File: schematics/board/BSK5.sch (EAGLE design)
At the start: 18 parts

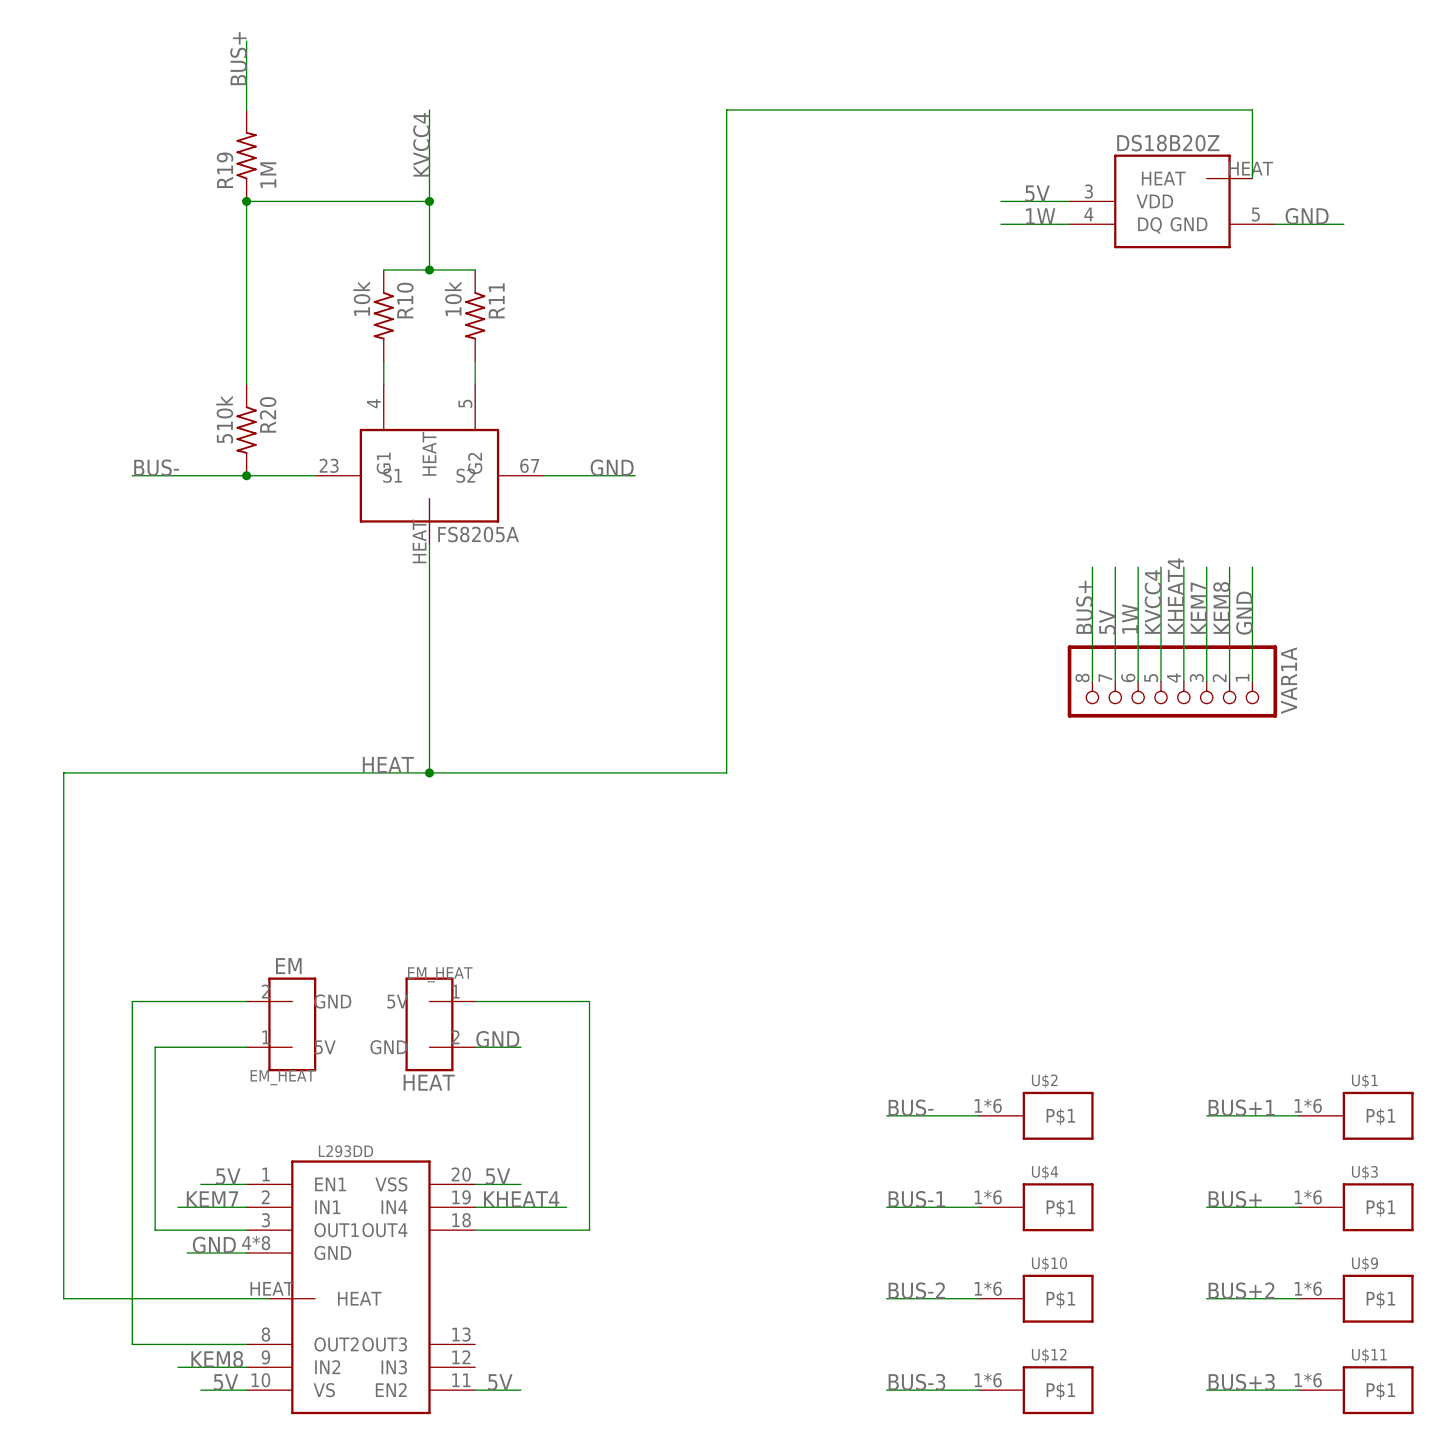
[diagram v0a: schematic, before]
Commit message: Добавлены светодиоды на платы БСК
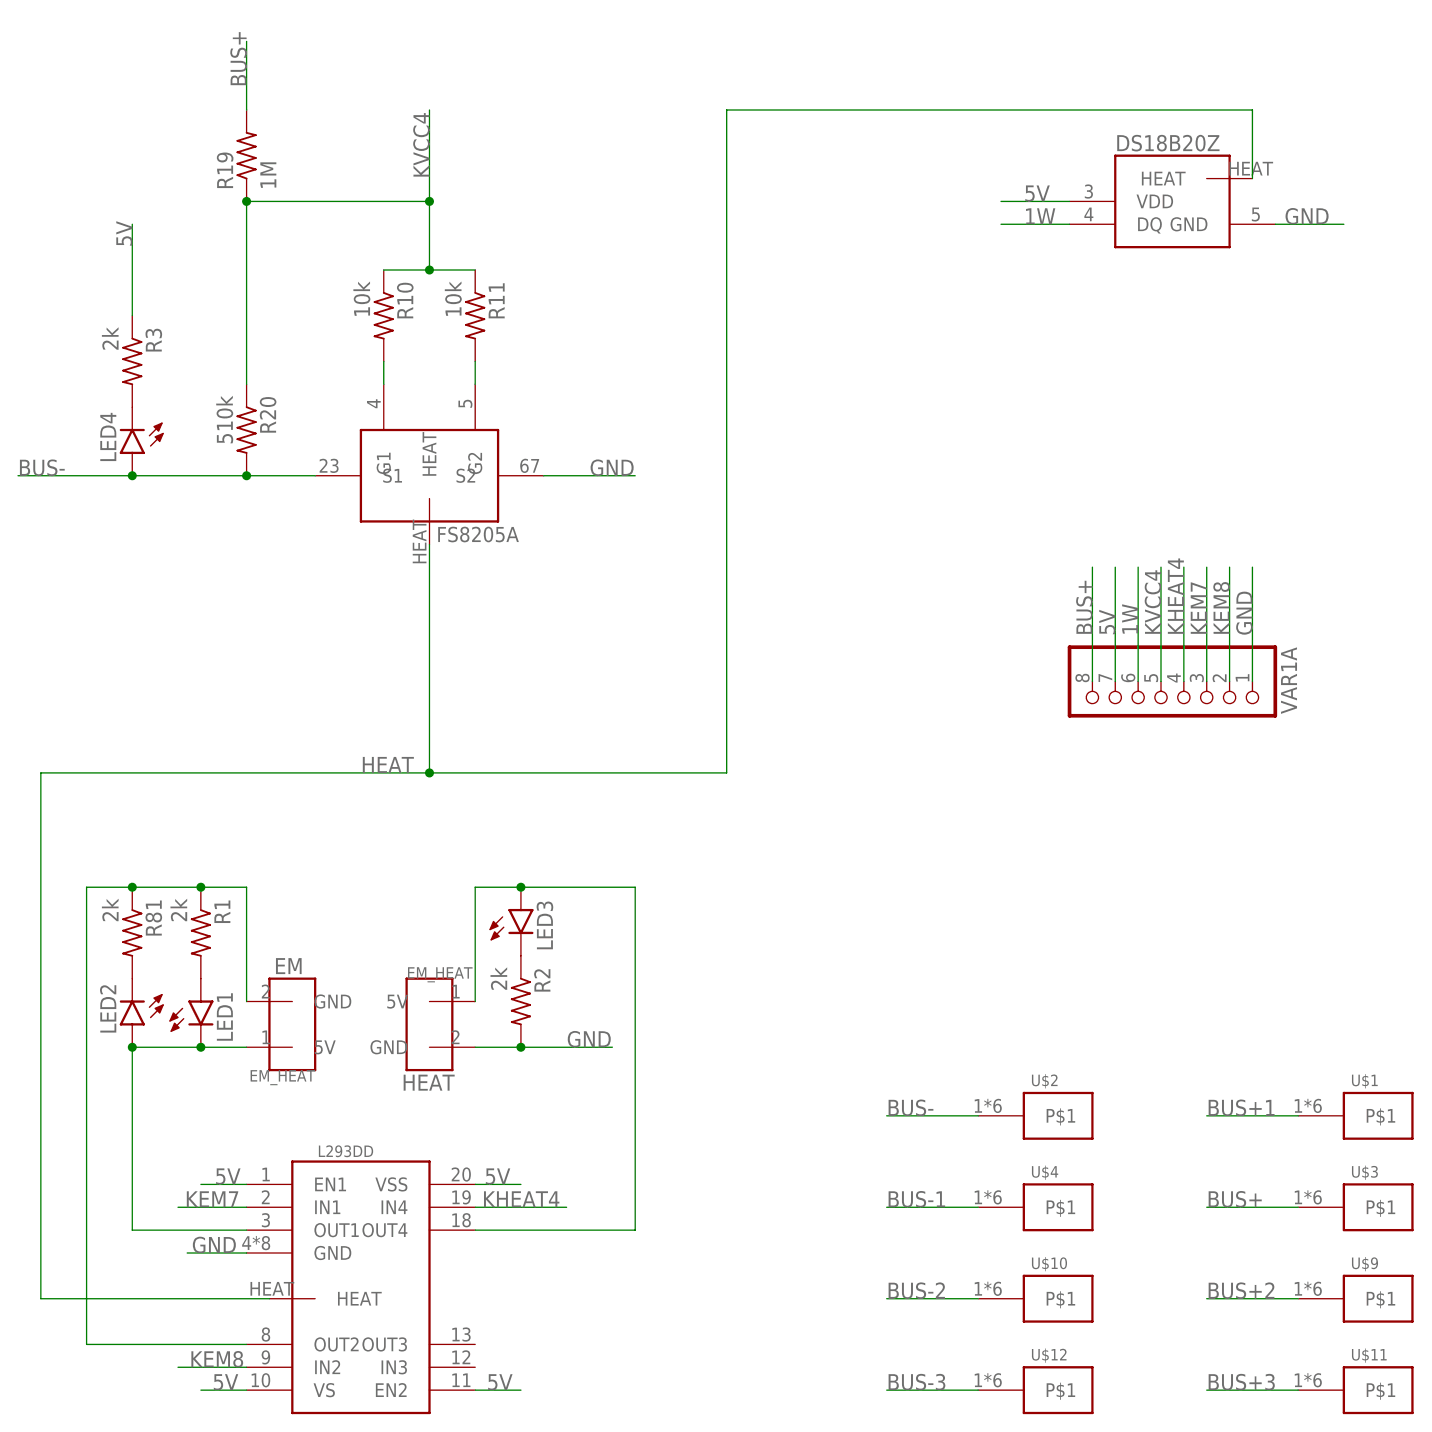
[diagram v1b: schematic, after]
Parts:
- added LED1, LED2, LED3, LED4: (no value), led:LEDCHIPLED_0603
- added R1, R2, R3, R81: 2k, resistor:R-US_R0603
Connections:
- new net N$26: LED2.C, R81.2
- new net N$27: LED1.A, R1.2
- new net N$28: LED3.C, R2.1
- new net N$29: LED4.C, R3.2
- net 5V: now also R3.1
- net BUS-: now also LED4.A
- net GND: now also R2.2
- net N$1: now also LED1.C, LED2.A
- net N$2: now also R1.1, R81.1
- net N$3: now also LED3.A
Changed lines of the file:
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@@
 <part name="U$12" library="CanCubeSat" deviceset="KCONNECT" device=""/>
 <part name="VAR1A" library="pinheadCS" deviceset="PINHD-1X8" device=""/>
+<part name="LED2" library="led" library_urn="urn:adsk.eagle:library:259" deviceset="LED" device="CHIPLED_0603" package3d_urn="urn:adsk.eagle:package:15822/2"/>
+<part name="R81" library="resistor" library_urn="urn:adsk.eagle:library:348" deviceset="R-US_" device="R0603" package3d_urn="urn:adsk.eagle:package:23555/3" value="2k"/>
+<part name="R1" library="resistor" library_urn="urn:adsk.eagle:library:348" deviceset="R-US_" device="R0603" package3d_urn="urn:adsk.eagle:package:23555/3" value="2k"/>
+<part name="LED1" library="led" library_urn="urn:adsk.eagle:library:259" deviceset="LED" device="CHIPLED_0603" package3d_urn="urn:adsk.eagle:package:15822/2"/>
+<part name="R2" library="resistor" library_urn="urn:adsk.eagle:library:348" deviceset="R-US_" device="R0603" package3d_urn="urn:adsk.eagle:package:23555/3" value="2k"/>
+<part name="LED3" library="led" library_urn="urn:adsk.eagle:library:259" deviceset="LED" device="CHIPLED_0603" package3d_urn="urn:adsk.eagle:package:15822/2"/>
+<part name="LED4" library="led" library_urn="urn:adsk.eagle:library:259" deviceset="LED" device="CHIPLED_0603" package3d_urn="urn:adsk.eagle:package:15822/2"/>
+<part name="R3" library="resistor" library_urn="urn:adsk.eagle:library:348" deviceset="R-US_" device="R0603" package3d_urn="urn:adsk.eagle:package:23555/3" value="2k"/>
 </parts>
 <sheets>
@@
 <attribute name="VALUE" x="142.24" y="181.61" size="1.778" layer="96" rot="R270"/>
 </instance>
+<instance part="LED2" gate="G$1" x="40.64" y="139.7" smashed="yes" rot="R180">
+<attribute name="NAME" x="37.084" y="144.272" size="1.778" layer="95" rot="R270"/>
+<attribute name="VALUE" x="34.925" y="144.272" size="1.778" layer="96" rot="R270"/>
+</instance>
+<instance part="R81" gate="G$1" x="40.64" y="149.86" smashed="yes" rot="R270">
+<attribute name="NAME" x="42.1386" y="153.67" size="1.778" layer="95" rot="R270"/>
+<attribute name="VALUE" x="37.338" y="153.67" size="1.778" layer="96" rot="R270"/>
+</instance>
+<instance part="R1" gate="G$1" x="48.26" y="149.86" smashed="yes" rot="R270">
+<attribute name="NAME" x="49.7586" y="153.67" size="1.778" layer="95" rot="R270"/>
+<attribute name="VALUE" x="44.958" y="153.67" size="1.778" layer="96" rot="R270"/>
+</instance>
+<instance part="LED1" gate="G$1" x="48.26" y="142.24" smashed="yes">
+<attribute name="NAME" x="51.816" y="137.668" size="1.778" layer="95" rot="R90"/>
+<attribute name="VALUE" x="53.975" y="137.668" size="1.778" layer="96" rot="R90"/>
+</instance>
+<instance part="R2" gate="G$1" x="83.82" y="142.24" smashed="yes" rot="R270">
+<attribute name="NAME" x="85.3186" y="146.05" size="1.778" layer="95" rot="R270"/>
+<attribute name="VALUE" x="80.518" y="146.05" size="1.778" layer="96" rot="R270"/>
+</instance>
+<instance part="LED3" gate="G$1" x="83.82" y="152.4" smashed="yes">
+<attribute name="NAME" x="87.376" y="147.828" size="1.778" layer="95" rot="R90"/>
+<attribute name="VALUE" x="89.535" y="147.828" size="1.778" layer="96" rot="R90"/>
+</instance>
+<instance part="LED4" gate="G$1" x="40.64" y="203.2" smashed="yes" rot="R180">
+<attribute name="NAME" x="37.084" y="207.772" size="1.778" layer="95" rot="R270"/>
+<attribute name="VALUE" x="34.925" y="207.772" size="1.778" layer="96" rot="R270"/>
+</instance>
+<instance part="R3" gate="G$1" x="40.64" y="213.36" smashed="yes" rot="R270">
+<attribute name="NAME" x="42.1386" y="217.17" size="1.778" layer="95" rot="R270"/>
+<attribute name="VALUE" x="37.338" y="217.17" size="1.778" layer="96" rot="R270"/>
+</instance>
 </instances>
 <busses>
@@
 <segment>
 <wire x1="78.74" y1="137.16" x2="83.82" y2="137.16" width="0.1524" layer="91"/>
-<label x="78.74" y="137.16" size="1.778" layer="95"/>
+<label x="88.9" y="137.16" size="1.778" layer="95"/>
 <pinref part="U$7" gate="G$1" pin="GND"/>
+<pinref part="R2" gate="G$1" pin="2"/>
+<wire x1="83.82" y1="137.16" x2="93.98" y2="137.16" width="0.1524" layer="91"/>
+<junction x="83.82" y="137.16"/>
 </segment>
 <segment>
@@
 <label x="139.7" y="231.14" size="1.778" layer="95"/>
 </segment>
+<segment>
+<pinref part="R3" gate="G$1" pin="1"/>
+<wire x1="40.64" y1="218.44" x2="40.64" y2="228.6" width="0.1524" layer="91"/>
+<label x="40.64" y="226.06" size="1.778" layer="95" rot="R90"/>
+</segment>
 </net>
 <net name="1W" class="0">
@@
 <segment>
 <pinref part="U$6" gate="G$1" pin="5V"/>
-<wire x1="53.34" y1="137.16" x2="43.18" y2="137.16" width="0.1524" layer="91"/>
-<wire x1="43.18" y1="137.16" x2="43.18" y2="116.84" width="0.1524" layer="91"/>
+<wire x1="53.34" y1="137.16" x2="48.26" y2="137.16" width="0.1524" layer="91"/>
+<wire x1="48.26" y1="137.16" x2="40.64" y2="137.16" width="0.1524" layer="91"/>
+<wire x1="40.64" y1="137.16" x2="40.64" y2="116.84" width="0.1524" layer="91"/>
 <pinref part="U$8" gate="G$1" pin="OUT1"/>
-<wire x1="43.18" y1="116.84" x2="53.34" y2="116.84" width="0.1524" layer="91"/>
+<wire x1="40.64" y1="116.84" x2="53.34" y2="116.84" width="0.1524" layer="91"/>
+<pinref part="LED2" gate="G$1" pin="A"/>
+<junction x="40.64" y="137.16"/>
+<pinref part="LED1" gate="G$1" pin="C"/>
+<junction x="48.26" y="137.16"/>
 </segment>
 </net>
 <net name="N$2" class="0">
 <segment>
+<wire x1="35.56" y1="154.94" x2="35.56" y2="104.14" width="0.1524" layer="91"/>
+<pinref part="U$8" gate="G$1" pin="OUT2"/>
+<wire x1="35.56" y1="104.14" x2="53.34" y2="104.14" width="0.1524" layer="91"/>
+<wire x1="35.56" y1="154.94" x2="40.64" y2="154.94" width="0.1524" layer="91"/>
 <pinref part="U$6" gate="G$1" pin="GND"/>
-<wire x1="53.34" y1="142.24" x2="40.64" y2="142.24" width="0.1524" layer="91"/>
-<wire x1="40.64" y1="142.24" x2="40.64" y2="104.14" width="0.1524" layer="91"/>
-<pinref part="U$8" gate="G$1" pin="OUT2"/>
-<wire x1="40.64" y1="104.14" x2="53.34" y2="104.14" width="0.1524" layer="91"/>
+<wire x1="40.64" y1="154.94" x2="48.26" y2="154.94" width="0.1524" layer="91"/>
+<wire x1="48.26" y1="154.94" x2="53.34" y2="154.94" width="0.1524" layer="91"/>
+<wire x1="53.34" y1="154.94" x2="53.34" y2="142.24" width="0.1524" layer="91"/>
+<pinref part="R81" gate="G$1" pin="1"/>
+<junction x="40.64" y="154.94"/>
+<pinref part="R1" gate="G$1" pin="1"/>
+<junction x="48.26" y="154.94"/>
 </segment>
 </net>
 <net name="N$3" class="0">
 <segment>
+<wire x1="96.52" y1="154.94" x2="96.52" y2="116.84" width="0.1524" layer="91"/>
+<pinref part="U$8" gate="G$1" pin="OUT4"/>
+<wire x1="96.52" y1="116.84" x2="78.74" y2="116.84" width="0.1524" layer="91"/>
 <pinref part="U$7" gate="G$1" pin="5V"/>
-<wire x1="78.74" y1="142.24" x2="91.44" y2="142.24" width="0.1524" layer="91"/>
-<wire x1="91.44" y1="142.24" x2="91.44" y2="116.84" width="0.1524" layer="91"/>
-<pinref part="U$8" gate="G$1" pin="OUT4"/>
-<wire x1="91.44" y1="116.84" x2="78.74" y2="116.84" width="0.1524" layer="91"/>
+<wire x1="96.52" y1="154.94" x2="83.82" y2="154.94" width="0.1524" layer="91"/>
+<wire x1="83.82" y1="154.94" x2="78.74" y2="154.94" width="0.1524" layer="91"/>
+<wire x1="78.74" y1="154.94" x2="78.74" y2="142.24" width="0.1524" layer="91"/>
+<pinref part="LED3" gate="G$1" pin="A"/>
+<junction x="83.82" y="154.94"/>
 </segment>
 </net>
@@
 <wire x1="53.34" y1="200.66" x2="40.64" y2="200.66" width="0.1524" layer="91"/>
 <junction x="53.34" y="200.66"/>
-<label x="40.64" y="200.66" size="1.778" layer="95"/>
+<label x="27.94" y="200.66" size="1.778" layer="95"/>
+<pinref part="LED4" gate="G$1" pin="A"/>
+<wire x1="40.64" y1="200.66" x2="27.94" y2="200.66" width="0.1524" layer="91"/>
+<junction x="40.64" y="200.66"/>
 </segment>
 <segment>
@@
 <segment>
 <pinref part="U$8" gate="G$1" pin="HEAT"/>
-<wire x1="55.88" y1="109.22" x2="33.02" y2="109.22" width="0.1524" layer="91"/>
-<wire x1="33.02" y1="109.22" x2="33.02" y2="167.64" width="0.1524" layer="91"/>
-<wire x1="33.02" y1="167.64" x2="73.66" y2="167.64" width="0.1524" layer="91"/>
+<wire x1="55.88" y1="109.22" x2="30.48" y2="109.22" width="0.1524" layer="91"/>
+<wire x1="30.48" y1="109.22" x2="30.48" y2="167.64" width="0.1524" layer="91"/>
+<wire x1="30.48" y1="167.64" x2="73.66" y2="167.64" width="0.1524" layer="91"/>
 <pinref part="U$14" gate="G$1" pin="HEAT"/>
 <wire x1="73.66" y1="167.64" x2="73.66" y2="193.04" width="0.1524" layer="91"/>
@@
 </segment>
 </net>
+<net name="N$26" class="0">
+<segment>
+<pinref part="LED2" gate="G$1" pin="C"/>
+<pinref part="R81" gate="G$1" pin="2"/>
+</segment>
+</net>
+<net name="N$27" class="0">
+<segment>
+<pinref part="LED1" gate="G$1" pin="A"/>
+<pinref part="R1" gate="G$1" pin="2"/>
+</segment>
+</net>
+<net name="N$28" class="0">
+<segment>
+<pinref part="LED3" gate="G$1" pin="C"/>
+<pinref part="R2" gate="G$1" pin="1"/>
+</segment>
+</net>
+<net name="N$29" class="0">
+<segment>
+<pinref part="LED4" gate="G$1" pin="C"/>
+<pinref part="R3" gate="G$1" pin="2"/>
+</segment>
+</net>
